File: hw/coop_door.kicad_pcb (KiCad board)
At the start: 2 copper layers, 110 x 110 mm, 53 parts, among them J1 Screw_Terminal_01x02, J2 Screw_Terminal_01x02, J3 Screw_Terminal_01x02, Q1 Q_NMOS_DDGSDD, Q2 IRF4905, Q3 Q_NMOS_DDGSDD, Q4 Q_Dual_NMOS_S1G1D2S2G2D1, Q5 Q_PMOS_DDGSDD, SW1 SW_Push, SW2 SW_DPDT_x2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

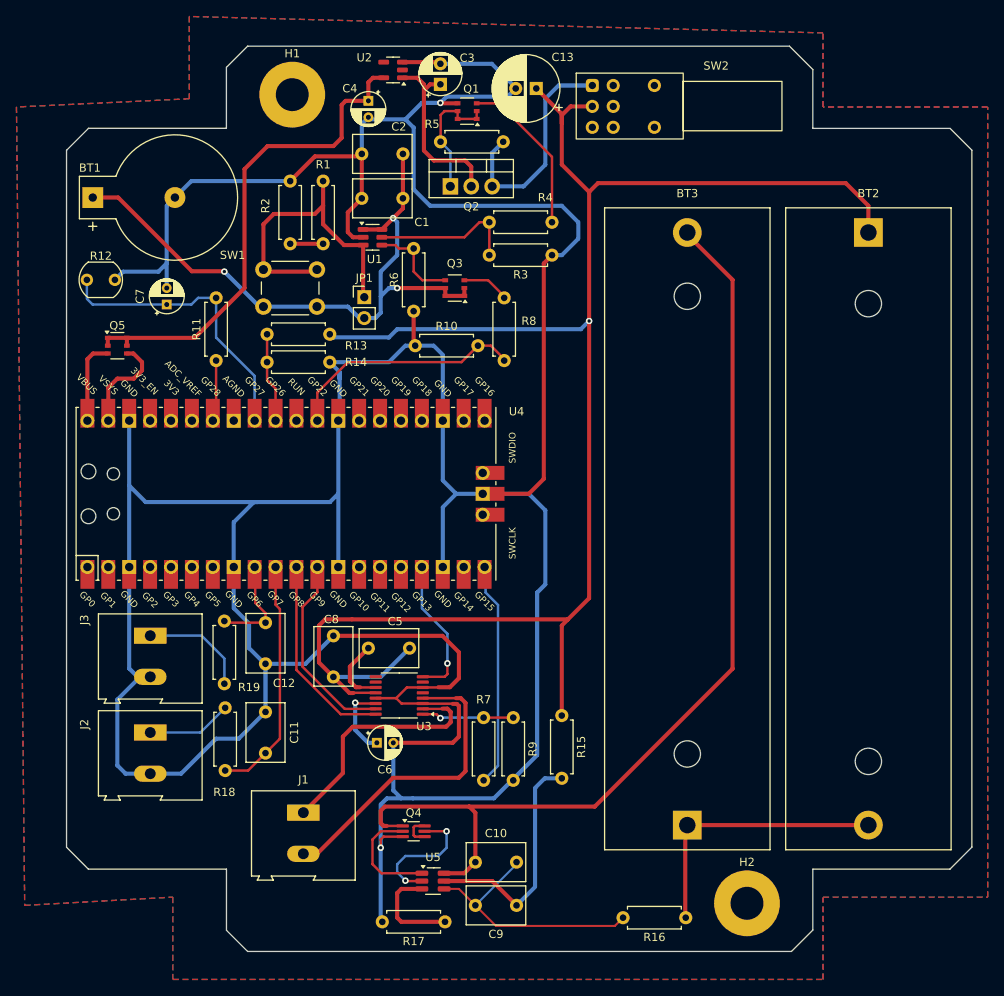
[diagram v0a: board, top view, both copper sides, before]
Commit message: Revise PCB dimensions
* Add project specific symbol library
* Change PCB dimensions to fit the housing
* Move some components for the connectors to be easily accessible
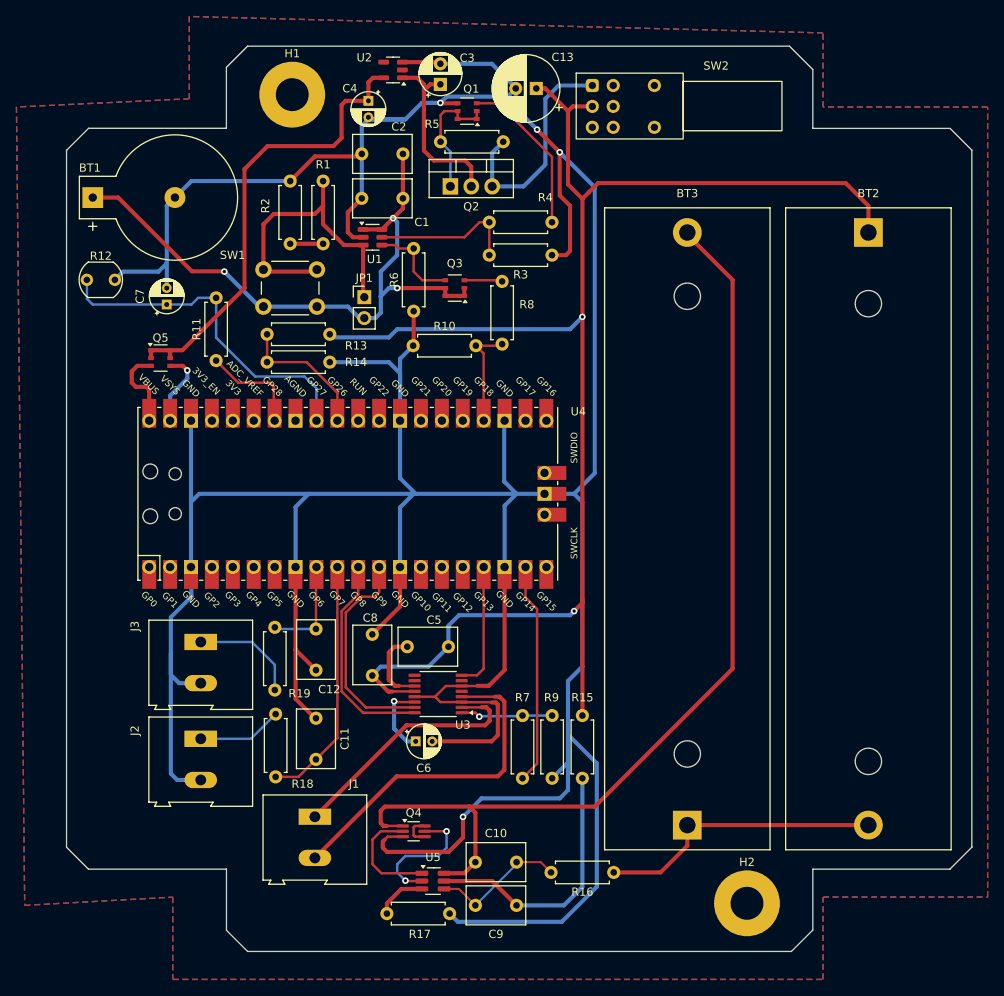
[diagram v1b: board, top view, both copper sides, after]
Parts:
- moved R16 10.3 mm to (150.3, 134.0)
- moved U4 7.51 mm to (118.0, 88.0)
- moved R17 7.13 mm to (122.8, 139.0), turned to 0 degrees
- moved R18 6.18 mm to (109.2, 122.4)
- moved C11 6.18 mm to (114.1, 120.3)
- moved C12 6.18 mm to (114.1, 104.4)
- moved J2 6.18 mm to (100.1, 117.8)
- moved J3 6.18 mm to (100.1, 106.0)
- moved R19 6.18 mm to (109.1, 104.2)
- moved Q5 5.46 mm to (95.2, 71.5)
- moved R7 4.73 mm to (139.2, 114.9)
- moved R9 4.73 mm to (142.8, 114.9)
- moved C6 4.73 mm to (126.3, 118.1)
- moved C5 4.73 mm to (130.2, 106.6)
- moved C8 4.73 mm to (121.0, 105.1)
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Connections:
- U4 pad 19: unconnected-(U4-GPIO14-Pad19) -> /motor_drv_nSLEEP
- U4 pad 20: /motor_drv_nSLEEP -> unconnected-(U4-GPIO15-Pad20)
- U4 pad 24: unconnected-(U4-GPIO18-Pad24) -> /done
- U4 pad 29: /done -> unconnected-(U4-GPIO22-Pad29)
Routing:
- net +BATT: track 210.8 -> 191.2 mm, vias 1 -> 2
- net GND: track 515.4 -> 533.1 mm, vias 2 -> 4
- net /done: track 29.1 -> 12.8 mm
- net Net-(U5-VC): track 31.3 -> 16.7 mm
- net /light_sense: track 35.5 -> 42.1 mm
- net /battery_sense: track 10.9 -> 17.1 mm
- net Net-(U5-VM): track 12.0 -> 6.22 mm
- net VCC: track 60.6 -> 56.0 mm
- net /motor_drv_AOUT2: track 37.6 -> 41.2 mm
- net Net-(U5-VDD): track 28.9 -> 32.1 mm
- net unconnected-(U4-3V3_EN-Pad37): track 0.00 -> 3.08 mm
- net /VSYS: track 12.3 -> 9.29 mm, vias 0 -> 1
- net /motor_drv_AIN2: track 23.9 -> 26.6 mm
- net /light_sense_control: track 9.98 -> 12.5 mm
- net /motor_drv_nFAULT: track 17.4 -> 15.6 mm, vias 1 -> 0
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
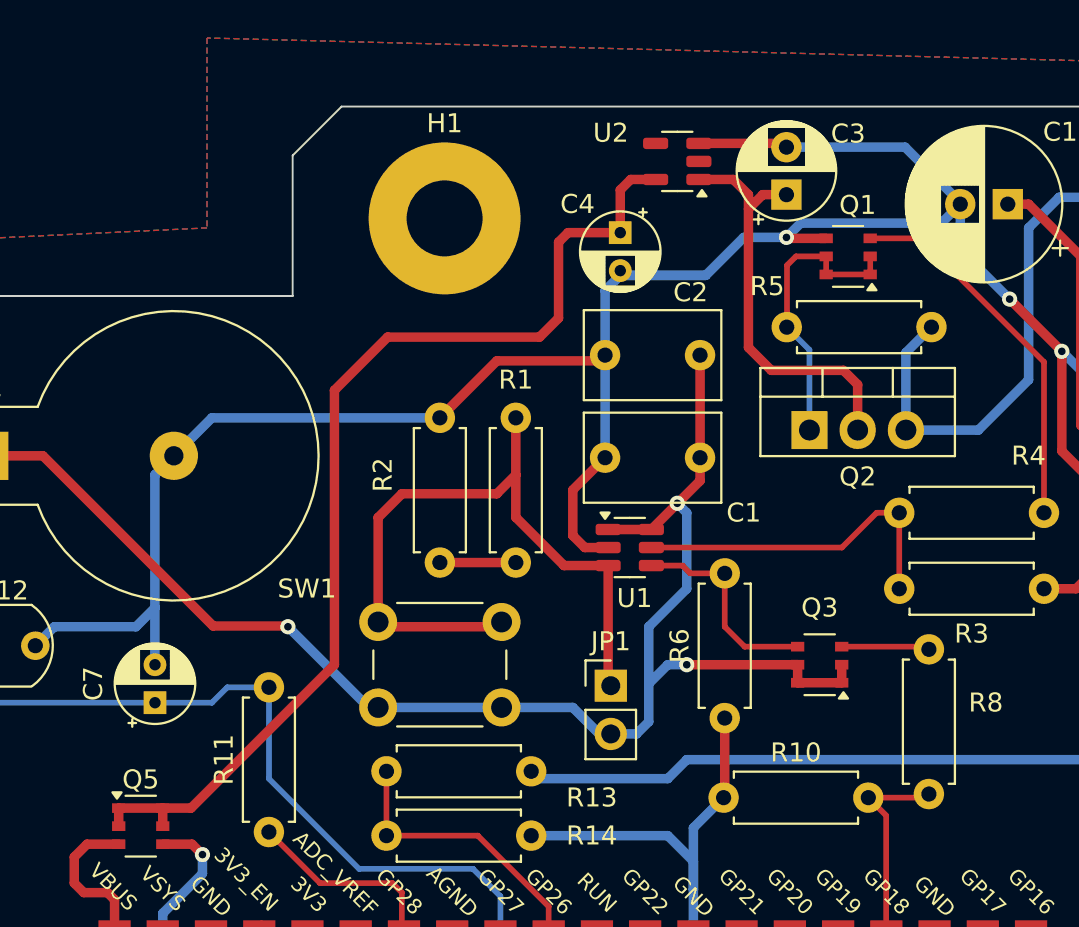
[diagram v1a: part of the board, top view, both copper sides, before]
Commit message: V-regulator
Use a correct symbol and package for TPS76633 voltage regulator.
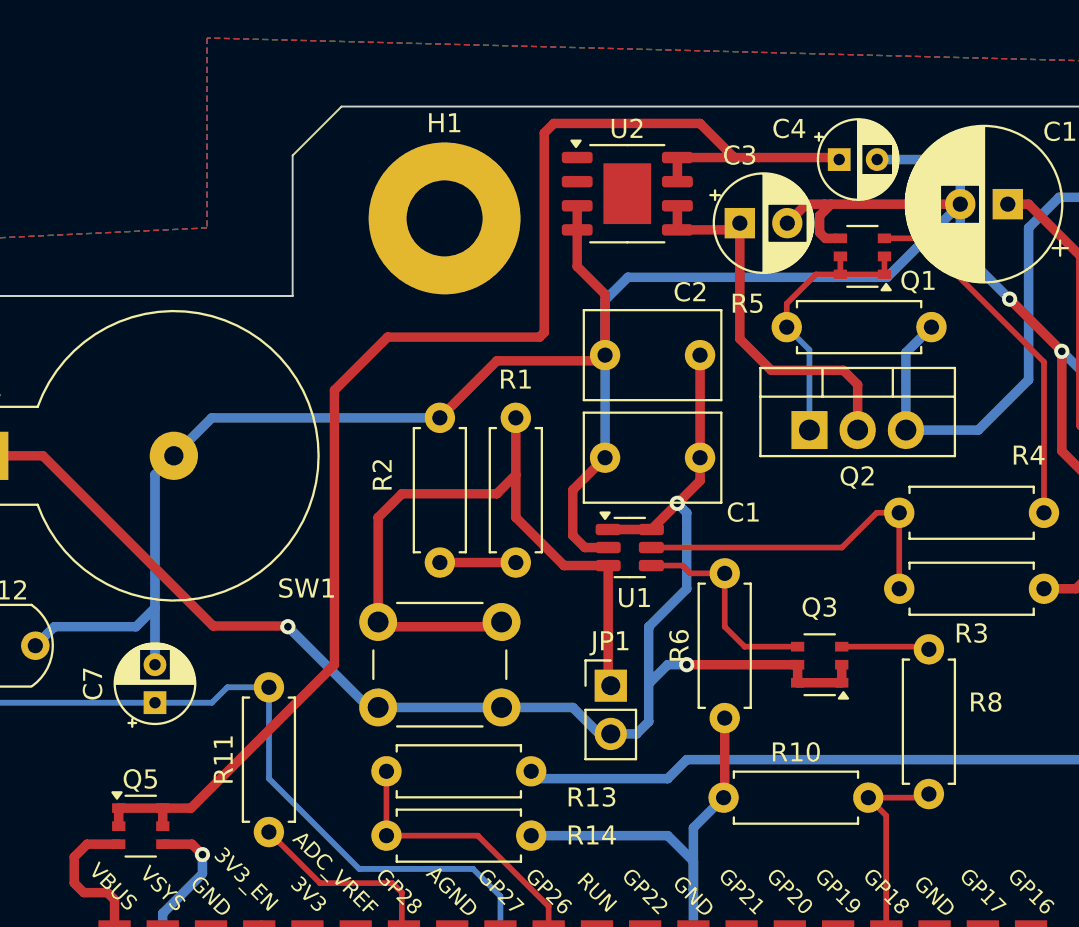
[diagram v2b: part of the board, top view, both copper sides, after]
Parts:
- U2: value TPS76333 -> TPS76633; footprint Package_TO_SOT_SMD:SOT-23-5 -> Package_SO:SOIC-8-1EP_3.9x4.9mm_P1.27mm_EP2.514x3.2mm
- moved C4 12.2 mm to (132.0, 36.4), turned to 0 degrees
- moved U2 3.13 mm to (120.9, 38.2), turned to 0 degrees
- moved C3 2.88 mm to (126.8, 39.8), turned to 0 degrees
- moved Q1 0.75 mm to (133.2, 41.5)
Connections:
- U2 pad 1: /VIN -> unconnected-(U2-NC-Pad1)
- U2 pad 2: GND -> unconnected-(U2-PG-Pad2)
- U2 pad 4: unconnected-(U2-NC-Pad4) -> GND
- U2 pad 5: VCC -> /VIN
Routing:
- net VCC: track 56.0 -> 74.2 mm
- net GND: track 533.1 -> 538.1 mm, vias 4 -> 3
- net /VIN: track 22.8 -> 21.0 mm
- net Net-(Q2-G): track 16.5 -> 14.9 mm
- net Net-(Q1-G): track 19.8 -> 19.0 mm

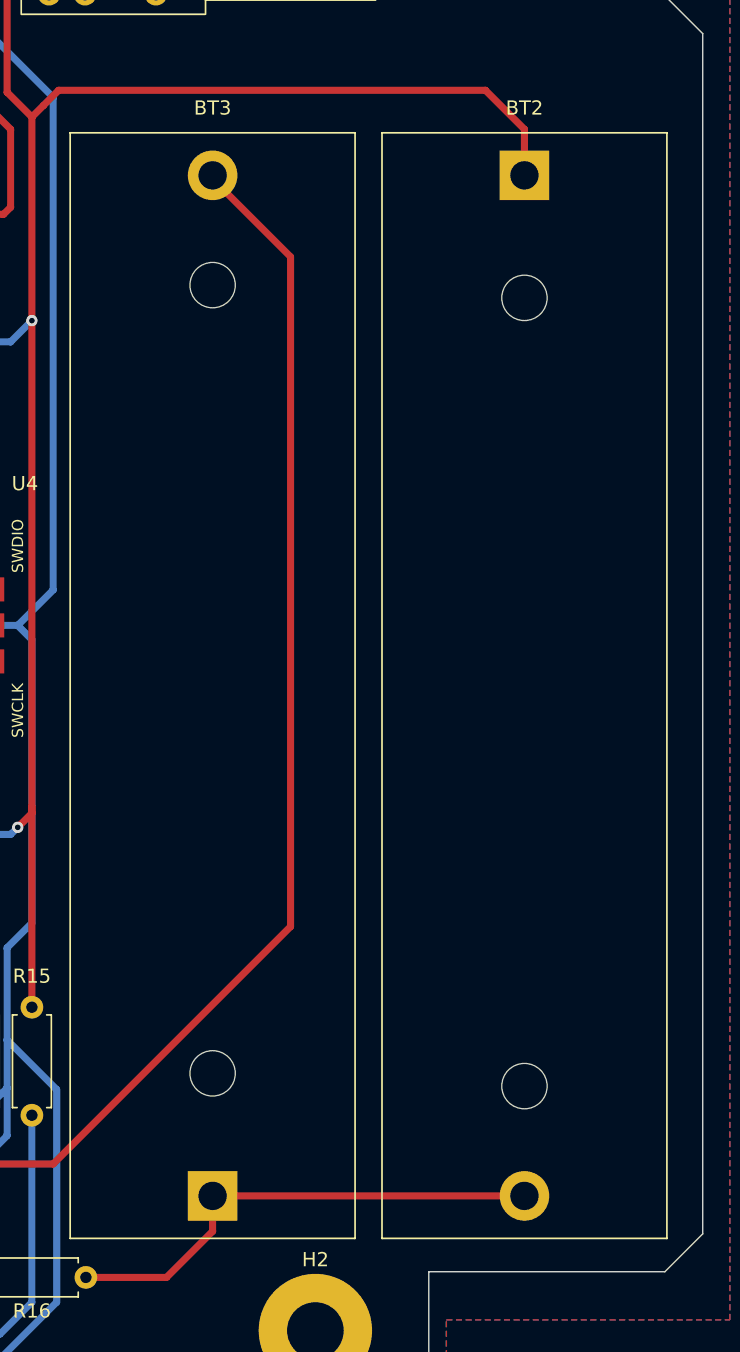
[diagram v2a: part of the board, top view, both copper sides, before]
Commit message: Battery terminals
Adding labels +/- to battery holders.
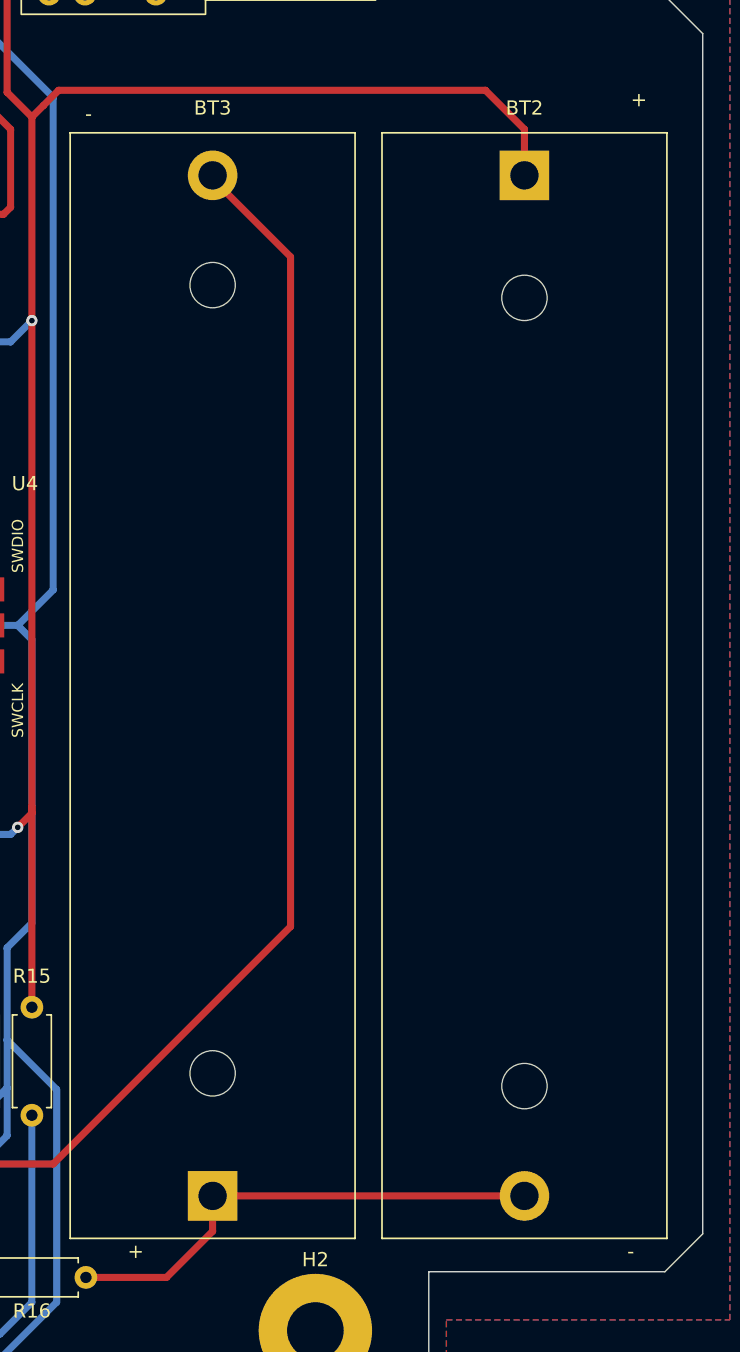
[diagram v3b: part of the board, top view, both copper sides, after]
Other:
- board text added: "+"
- board text added: "-"
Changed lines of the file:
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@@
     (effects (font (size 3 3) (thickness 0.75) bold) (justify left bottom mirror))
+  )
+  (gr_text "+" (at 153.25 132.75) (layer "F.SilkS")
+    (effects (font (size 1 1) (thickness 0.15)) (justify left bottom))
+  )
+  (gr_text "+" (at 188.75 51.5) (layer "F.SilkS")
+    (effects (font (size 1 1) (thickness 0.15)) (justify left bottom))
+  )
+  (gr_text "-" (at 188.5 132.75) (layer "F.SilkS")
+    (effects (font (size 1 1) (thickness 0.15)) (justify left bottom))
+  )
+  (gr_text "-" (at 150.25 52.5) (layer "F.SilkS")
+    (effects (font (size 1 1) (thickness 0.15)) (justify left bottom))
   )
   (segment (start 132.16 63.95) (end 129.84 63.95) (width 0.5) (layer "F.Cu") (net 1))

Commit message: PCB fixes
- Fix the battery protection IC MOSFET connections
- Add the main switch ON/OFF silkscreen labels
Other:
- board text added: "OFF"
- board text added: "ON"
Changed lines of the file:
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@@
     (effects (font (size 3 3) (thickness 0.75) bold) (justify left bottom mirror))
   )
+  (gr_text "OFF" (at 168.5 35.75) (layer "F.SilkS")
+    (effects (font (size 1 1) (thickness 0.15)) (justify left bottom))
+  )
   (gr_text "+" (at 153.25 132.75) (layer "F.SilkS")
     (effects (font (size 1 1) (thickness 0.15)) (justify left bottom))
@@
   )
   (gr_text "-" (at 150.25 52.5) (layer "F.SilkS")
+    (effects (font (size 1 1) (thickness 0.15)) (justify left bottom))
+  )
+  (gr_text "ON" (at 168.5 47.25) (layer "F.SilkS")
     (effects (font (size 1 1) (thickness 0.15)) (justify left bottom))
   )
@@
     (connect_pads (clearance 0.5))
     (min_thickness 0.25) (filled_areas_thickness no)
-    (fill yes (thermal_gap 0.5) (thermal_bridge_width 0.5))
+    (fill (thermal_gap 0.5) (thermal_bridge_width 0.5))
     (polygon
       (pts

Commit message: Termials labels
Add labels to end switch and motor terminals.
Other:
- board text added: "CLOSE END SW"
- board text added: "MOTOR"
- board text added: "OPEN END SW"
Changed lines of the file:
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@@
     (effects (font (size 3 3) (thickness 0.75) bold) (justify left bottom mirror))
+  )
+  (gr_text "OPEN \nEND SW" (at 90.75 121 90) (layer "F.SilkS")
+    (effects (font (size 1 1) (thickness 0.15)) (justify bottom))
   )
   (gr_text "OFF" (at 168.5 35.75) (layer "F.SilkS")
@@
     (effects (font (size 1 1) (thickness 0.15)) (justify left bottom))
   )
+  (gr_text "CLOSE \nEND SW" (at 90.5 108.75 90) (layer "F.SilkS")
+    (effects (font (size 1 1) (thickness 0.15)) (justify bottom))
+  )
+  (gr_text "MOTOR" (at 106.25 133 90) (layer "F.SilkS")
+    (effects (font (size 1 1) (thickness 0.15)) (justify left bottom))
+  )
